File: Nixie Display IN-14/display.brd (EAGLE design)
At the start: 112.6 x 51.6 mm, 22 parts, among them U1 TPIC6B595DWRG4, U2 TPIC6B595DWRG4, U3 TPIC6B595DWRG4, U4 TPIC6B595DWRG4, U5 TPIC6B595DWRG4, X1 22-23-2021

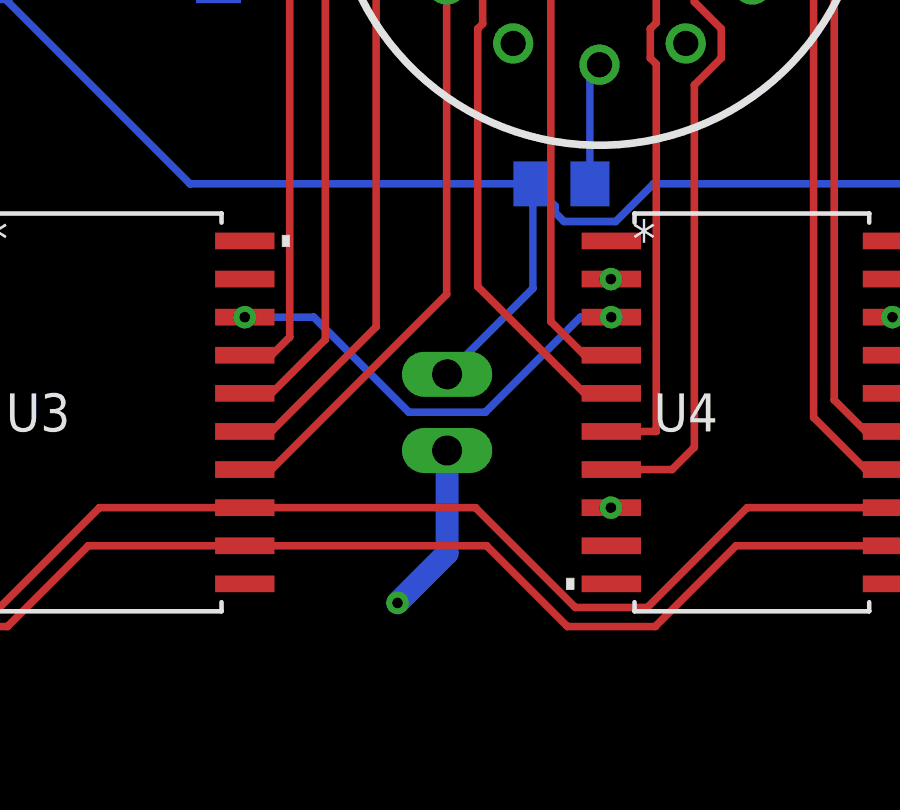
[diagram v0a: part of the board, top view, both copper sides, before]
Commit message: Begins sketch, fixes spacing and encoder circuit
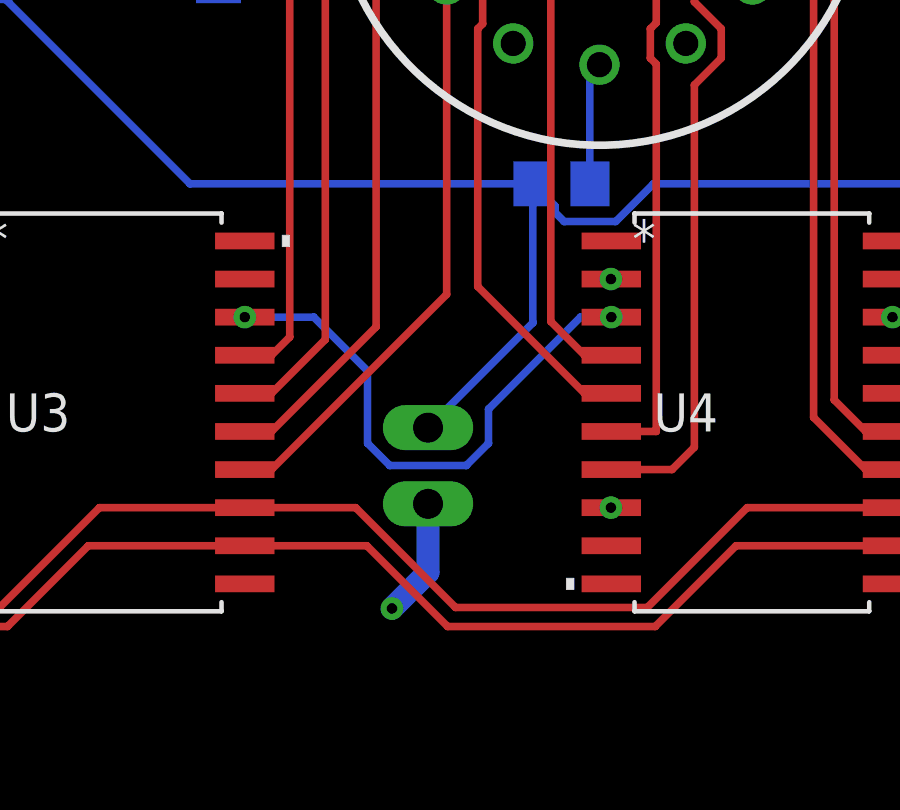
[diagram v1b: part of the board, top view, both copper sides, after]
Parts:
- moved X1 1.89 mm to (67.1, 14.9)
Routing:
- net N$79: track 14.8 -> 18.4 mm
- net V+: track 92.3 -> 94.3 mm
- net GND: track 19.6 -> 17.8 mm
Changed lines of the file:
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@@
 <attribute name="VALUE" x="14.097" y="6.731" size="1.27" layer="27" ratio="10" rot="R180"/>
 </element>
-<element name="X1" library="con-molex" library_urn="urn:adsk.eagle:library:165" package="22-23-2021" package3d_urn="urn:adsk.eagle:package:8078633/1" value="22-23-2021" x="67.691" y="16.637" smashed="yes" rot="MR270">
-<attribute name="MF" value="MOLEX" x="67.691" y="16.637" size="1.778" layer="28" rot="MR270" display="off"/>
-<attribute name="MPN" value="22-23-2021" x="67.691" y="16.637" size="1.778" layer="28" rot="MR270" display="off"/>
-<attribute name="NAME" x="63.881" y="19.177" size="1.016" layer="26" ratio="10" rot="MR270"/>
-<attribute name="OC_FARNELL" value="1462926" x="67.691" y="16.637" size="1.778" layer="28" rot="MR270" display="off"/>
-<attribute name="OC_NEWARK" value="25C3832" x="67.691" y="16.637" size="1.778" layer="28" rot="MR270" display="off"/>
-<attribute name="POPULARITY" value="40" x="67.691" y="16.637" size="1.778" layer="28" rot="MR270" display="off"/>
-<attribute name="VALUE" x="72.771" y="19.177" size="1.016" layer="28" ratio="10" rot="MR270"/>
+<element name="X1" library="con-molex" library_urn="urn:adsk.eagle:library:165" package="22-23-2021" package3d_urn="urn:adsk.eagle:package:8078633/1" value="22-23-2021" x="67.056" y="14.859" smashed="yes" rot="MR270">
+<attribute name="MF" value="MOLEX" x="67.056" y="14.859" size="1.778" layer="28" rot="MR270" display="off"/>
+<attribute name="MPN" value="22-23-2021" x="67.056" y="14.859" size="1.778" layer="28" rot="MR270" display="off"/>
+<attribute name="NAME" x="63.246" y="17.399" size="1.016" layer="26" ratio="10" rot="MR270"/>
+<attribute name="OC_FARNELL" value="1462926" x="67.056" y="14.859" size="1.778" layer="28" rot="MR270" display="off"/>
+<attribute name="OC_NEWARK" value="25C3832" x="67.056" y="14.859" size="1.778" layer="28" rot="MR270" display="off"/>
+<attribute name="POPULARITY" value="40" x="67.056" y="14.859" size="1.778" layer="28" rot="MR270" display="off"/>
+<attribute name="VALUE" x="72.136" y="17.399" size="1.016" layer="28" ratio="10" rot="MR270"/>
 </element>
 </elements>
@@
 <contactref element="U1" pad="10"/>
 <contactref element="U1" pad="9"/>
-<wire x1="67.691" y1="15.367" x2="67.691" y2="11.938" width="0.762" layer="16"/>
-<wire x1="67.691" y1="11.938" x2="66.04" y2="10.287" width="0.762" layer="16"/>
-<via x="66.04" y="10.287" extent="1-16" drill="0.35"/>
+<wire x1="67.056" y1="13.589" x2="67.056" y2="11.303" width="0.762" layer="16"/>
 <via x="39.3573" y="21.082" extent="1-16" drill="0.35"/>
 <wire x1="39.3573" y1="21.082" x2="42.926" y2="21.082" width="0.254" layer="16"/>
@@
 <wire x1="30.5915" y1="10.414" x2="34.036" y2="10.414" width="0.254" layer="16"/>
 <via x="34.036" y="10.414" extent="1-16" drill="0.35"/>
+<via x="65.853971875" y="10.100971875" extent="1-16" drill="0.35"/>
+<wire x1="67.056" y1="11.303" x2="65.853971875" y2="10.100971875" width="0.762" layer="16"/>
 </signal>
 <signal name="VCC">
@@
 <wire x1="74.56941875" y1="24.257" x2="94.681" y2="24.257" width="0.254" layer="16"/>
 <wire x1="73.31141875" y1="22.999" x2="74.56941875" y2="24.257" width="0.254" layer="16"/>
-<wire x1="70.551" y1="24.257" x2="70.551" y2="20.767" width="0.254" layer="16"/>
-<wire x1="70.551" y1="20.767" x2="67.691" y2="17.907" width="0.254" layer="16"/>
+<wire x1="70.551" y1="24.257" x2="70.551" y2="19.624" width="0.254" layer="16"/>
+<wire x1="70.551" y1="19.624" x2="67.056" y2="16.129" width="0.254" layer="16"/>
 </signal>
 <signal name="N$21">
@@
 <via x="60.9473" y="19.812" extent="1-16" drill="0.35"/>
 <via x="73.1647" y="19.812" extent="1-16" drill="0.35"/>
-<wire x1="66.41425625" y1="16.645" x2="68.96774375" y2="16.645" width="0.254" layer="16"/>
-<wire x1="60.9473" y1="19.812" x2="63.24725625" y2="19.812" width="0.254" layer="16"/>
+<wire x1="60.9473" y1="19.812" x2="63.246" y2="19.812" width="0.254" layer="16"/>
+<wire x1="63.246" y1="19.812" x2="63.24725625" y2="19.812" width="0.254" layer="16"/>
 <wire x1="72.13474375" y1="19.812" x2="73.1647" y2="19.812" width="0.254" layer="16"/>
-<wire x1="63.24725625" y1="19.812" x2="66.41425625" y2="16.645" width="0.254" layer="16"/>
-<wire x1="68.96774375" y1="16.645" x2="72.13474375" y2="19.812" width="0.254" layer="16"/>
+<wire x1="65.04" y1="15.60625625" x2="65.77925625" y2="14.867" width="0.254" layer="16"/>
+<wire x1="65.77925625" y1="14.867" x2="68.33274375" y2="14.867" width="0.254" layer="16"/>
+<wire x1="68.33274375" y1="14.867" x2="69.072" y2="15.60625625" width="0.254" layer="16"/>
+<wire x1="69.072" y1="15.60625625" x2="69.072" y2="16.74925625" width="0.254" layer="16"/>
+<wire x1="69.072" y1="16.74925625" x2="72.13474375" y2="19.812" width="0.254" layer="16"/>
+<wire x1="63.246" y1="19.812" x2="65.04" y2="18.018" width="0.254" layer="16"/>
+<wire x1="65.04" y1="18.018" x2="65.04" y2="15.60625625" width="0.254" layer="16"/>
 </signal>
 <signal name="N$27">
@@
 <wire x1="50.11065" y1="9.4996" x2="53.03875" y2="9.4996" width="0.254" layer="1"/>
 <wire x1="53.03875" y1="9.4996" x2="55.73115" y2="12.192" width="0.254" layer="1"/>
-<wire x1="60.9473" y1="12.192" x2="69.00825" y2="12.192" width="0.254" layer="1"/>
-<wire x1="69.00825" y1="12.192" x2="71.70065" y2="9.4996" width="0.254" layer="1"/>
 <wire x1="77.32115" y1="12.192" x2="82.5373" y2="12.192" width="0.254" layer="1"/>
-<wire x1="71.70065" y1="9.4996" x2="74.62875" y2="9.4996" width="0.254" layer="1"/>
 <wire x1="74.62875" y1="9.4996" x2="77.32115" y2="12.192" width="0.254" layer="1"/>
 <wire x1="82.5373" y1="12.192" x2="90.59825" y2="12.192" width="0.254" layer="1"/>
@@
 <wire x1="16.637" y1="3.81" x2="17.018" y2="4.191" width="0.254" layer="1"/>
 <wire x1="17.018" y1="9.68288125" x2="16.2687" y2="10.43218125" width="0.254" layer="1"/>
+<wire x1="60.9473" y1="12.192" x2="65.016225" y2="12.192" width="0.254" layer="1"/>
+<wire x1="65.016225" y1="12.192" x2="67.708625" y2="9.4996" width="0.254" layer="1"/>
+<wire x1="67.708625" y1="9.4996" x2="74.62875" y2="9.4996" width="0.254" layer="1"/>
 </signal>
 <signal name="N$49">
@@
 <wire x1="47.04628125" y1="13.462" x2="50.37368125" y2="10.1346" width="0.254" layer="1"/>
 <wire x1="52.77571875" y1="10.1346" x2="56.10311875" y2="13.462" width="0.254" layer="1"/>
-<wire x1="71.96368125" y1="10.1346" x2="74.36571875" y2="10.1346" width="0.254" layer="1"/>
-<wire x1="60.9473" y1="13.462" x2="68.63628125" y2="13.462" width="0.254" layer="1"/>
 <wire x1="77.69311875" y1="13.462" x2="82.5373" y2="13.462" width="0.254" layer="1"/>
-<wire x1="68.63628125" y1="13.462" x2="71.96368125" y2="10.1346" width="0.254" layer="1"/>
 <wire x1="74.36571875" y1="10.1346" x2="77.69311875" y2="13.462" width="0.254" layer="1"/>
 <wire x1="93.55368125" y1="10.1346" x2="95.95571875" y2="10.1346" width="0.254" layer="1"/>
@@
 <wire x1="14.478" y1="10.89111875" x2="14.478" y2="4.191" width="0.254" layer="1"/>
 <wire x1="14.478" y1="4.191" x2="14.097" y2="3.81" width="0.254" layer="1"/>
+<wire x1="60.9473" y1="13.462" x2="64.64425625" y2="13.462" width="0.254" layer="1"/>
+<wire x1="64.64425625" y1="13.462" x2="67.97165625" y2="10.1346" width="0.254" layer="1"/>
+<wire x1="67.97165625" y1="10.1346" x2="74.36571875" y2="10.1346" width="0.254" layer="1"/>
 </signal>
 <signal name="N$52">

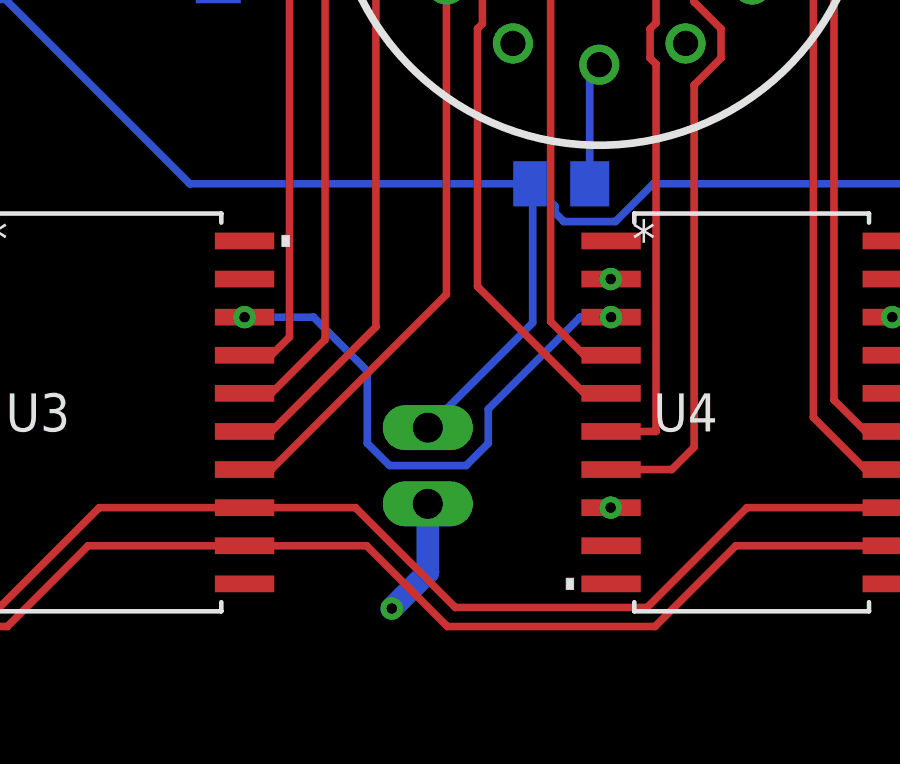
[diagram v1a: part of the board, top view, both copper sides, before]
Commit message: Tweaks design, adds arduino clock sketch
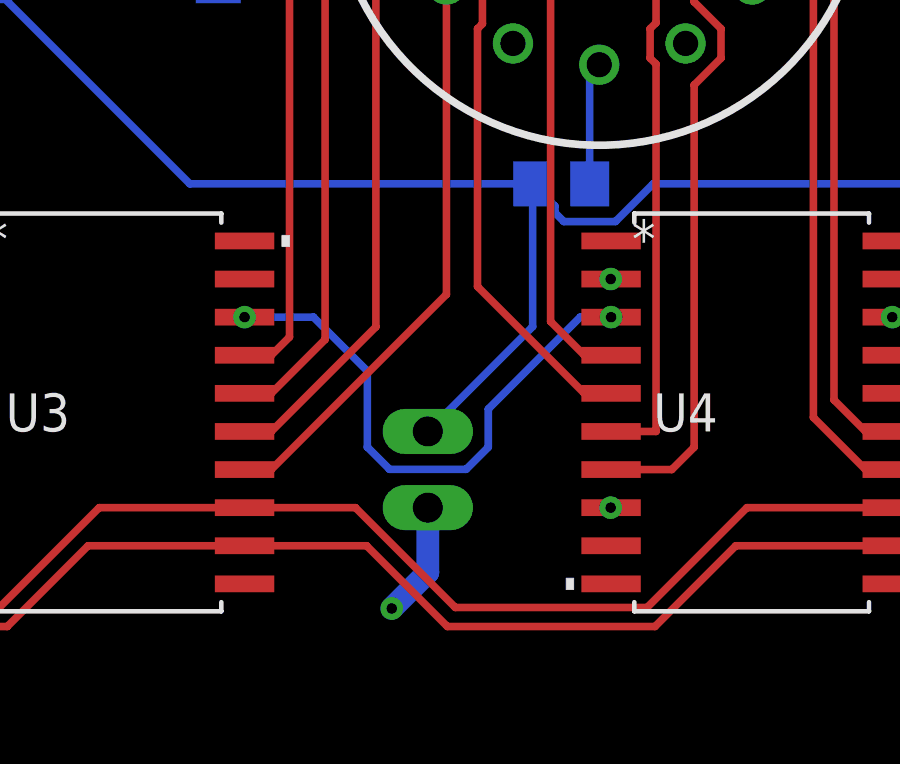
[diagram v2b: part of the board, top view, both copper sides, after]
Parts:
- moved X1 0.13 mm to (67.1, 14.7)
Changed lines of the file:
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@@
 <attribute name="VALUE" x="14.097" y="6.731" size="1.27" layer="27" ratio="10" rot="R180"/>
 </element>
-<element name="X1" library="con-molex" library_urn="urn:adsk.eagle:library:165" package="22-23-2021" package3d_urn="urn:adsk.eagle:package:8078633/1" value="22-23-2021" x="67.056" y="14.859" smashed="yes" rot="MR270">
-<attribute name="MF" value="MOLEX" x="67.056" y="14.859" size="1.778" layer="28" rot="MR270" display="off"/>
-<attribute name="MPN" value="22-23-2021" x="67.056" y="14.859" size="1.778" layer="28" rot="MR270" display="off"/>
-<attribute name="NAME" x="63.246" y="17.399" size="1.016" layer="26" ratio="10" rot="MR270"/>
-<attribute name="OC_FARNELL" value="1462926" x="67.056" y="14.859" size="1.778" layer="28" rot="MR270" display="off"/>
-<attribute name="OC_NEWARK" value="25C3832" x="67.056" y="14.859" size="1.778" layer="28" rot="MR270" display="off"/>
-<attribute name="POPULARITY" value="40" x="67.056" y="14.859" size="1.778" layer="28" rot="MR270" display="off"/>
-<attribute name="VALUE" x="72.136" y="17.399" size="1.016" layer="28" ratio="10" rot="MR270"/>
+<element name="X1" library="con-molex" library_urn="urn:adsk.eagle:library:165" package="22-23-2021" package3d_urn="urn:adsk.eagle:package:8078633/1" value="22-23-2021" x="67.056" y="14.732" locked="yes" smashed="yes" rot="MR270">
+<attribute name="MF" value="MOLEX" x="67.056" y="14.732" locked="yes" size="1.778" layer="28" rot="MR270" display="off"/>
+<attribute name="MPN" value="22-23-2021" x="67.056" y="14.732" locked="yes" size="1.778" layer="28" rot="MR270" display="off"/>
+<attribute name="NAME" x="63.246" y="17.272" locked="yes" size="1.016" layer="26" ratio="10" rot="MR270"/>
+<attribute name="OC_FARNELL" value="1462926" x="67.056" y="14.732" locked="yes" size="1.778" layer="28" rot="MR270" display="off"/>
+<attribute name="OC_NEWARK" value="25C3832" x="67.056" y="14.732" locked="yes" size="1.778" layer="28" rot="MR270" display="off"/>
+<attribute name="POPULARITY" value="40" x="67.056" y="14.732" locked="yes" size="1.778" layer="28" rot="MR270" display="off"/>
+<attribute name="VALUE" x="72.136" y="17.272" locked="yes" size="1.016" layer="28" ratio="10" rot="MR270"/>
 </element>
 </elements>
@@
 <contactref element="U1" pad="10"/>
 <contactref element="U1" pad="9"/>
-<wire x1="67.056" y1="13.589" x2="67.056" y2="11.303" width="0.762" layer="16"/>
+<wire x1="67.056" y1="13.462" x2="67.056" y2="11.303" width="0.762" layer="16"/>
 <via x="39.3573" y="21.082" extent="1-16" drill="0.35"/>
 <wire x1="39.3573" y1="21.082" x2="42.926" y2="21.082" width="0.254" layer="16"/>
@@
 <wire x1="74.56941875" y1="24.257" x2="94.681" y2="24.257" width="0.254" layer="16"/>
 <wire x1="73.31141875" y1="22.999" x2="74.56941875" y2="24.257" width="0.254" layer="16"/>
-<wire x1="70.551" y1="24.257" x2="70.551" y2="19.624" width="0.254" layer="16"/>
-<wire x1="70.551" y1="19.624" x2="67.056" y2="16.129" width="0.254" layer="16"/>
+<wire x1="70.551" y1="24.257" x2="70.551" y2="19.497" width="0.254" layer="16"/>
+<wire x1="70.551" y1="19.497" x2="67.056" y2="16.002" width="0.254" layer="16"/>
 </signal>
 <signal name="N$21">
@@
 <wire x1="63.246" y1="19.812" x2="63.24725625" y2="19.812" width="0.254" layer="16"/>
 <wire x1="72.13474375" y1="19.812" x2="73.1647" y2="19.812" width="0.254" layer="16"/>
-<wire x1="65.04" y1="15.60625625" x2="65.77925625" y2="14.867" width="0.254" layer="16"/>
-<wire x1="65.77925625" y1="14.867" x2="68.33274375" y2="14.867" width="0.254" layer="16"/>
-<wire x1="68.33274375" y1="14.867" x2="69.072" y2="15.60625625" width="0.254" layer="16"/>
-<wire x1="69.072" y1="15.60625625" x2="69.072" y2="16.74925625" width="0.254" layer="16"/>
 <wire x1="69.072" y1="16.74925625" x2="72.13474375" y2="19.812" width="0.254" layer="16"/>
 <wire x1="63.246" y1="19.812" x2="65.04" y2="18.018" width="0.254" layer="16"/>
-<wire x1="65.04" y1="18.018" x2="65.04" y2="15.60625625" width="0.254" layer="16"/>
+<wire x1="65.04" y1="15.47925625" x2="65.77925625" y2="14.74" width="0.254" layer="16"/>
+<wire x1="65.77925625" y1="14.74" x2="68.33274375" y2="14.74" width="0.254" layer="16"/>
+<wire x1="68.33274375" y1="14.74" x2="69.072" y2="15.47925625" width="0.254" layer="16"/>
+<wire x1="65.04" y1="18.018" x2="65.04" y2="15.47925625" width="0.254" layer="16"/>
+<wire x1="69.072" y1="15.47925625" x2="69.072" y2="16.74925625" width="0.254" layer="16"/>
 </signal>
 <signal name="N$27">
